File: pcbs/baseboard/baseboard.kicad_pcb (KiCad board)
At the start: 2 copper layers, 86 x 110 mm, 19 parts, among them J1 Power, J3 gpio_breakout, J4 SWD, J5 DC, SW1 SW_Push, U1 Pico

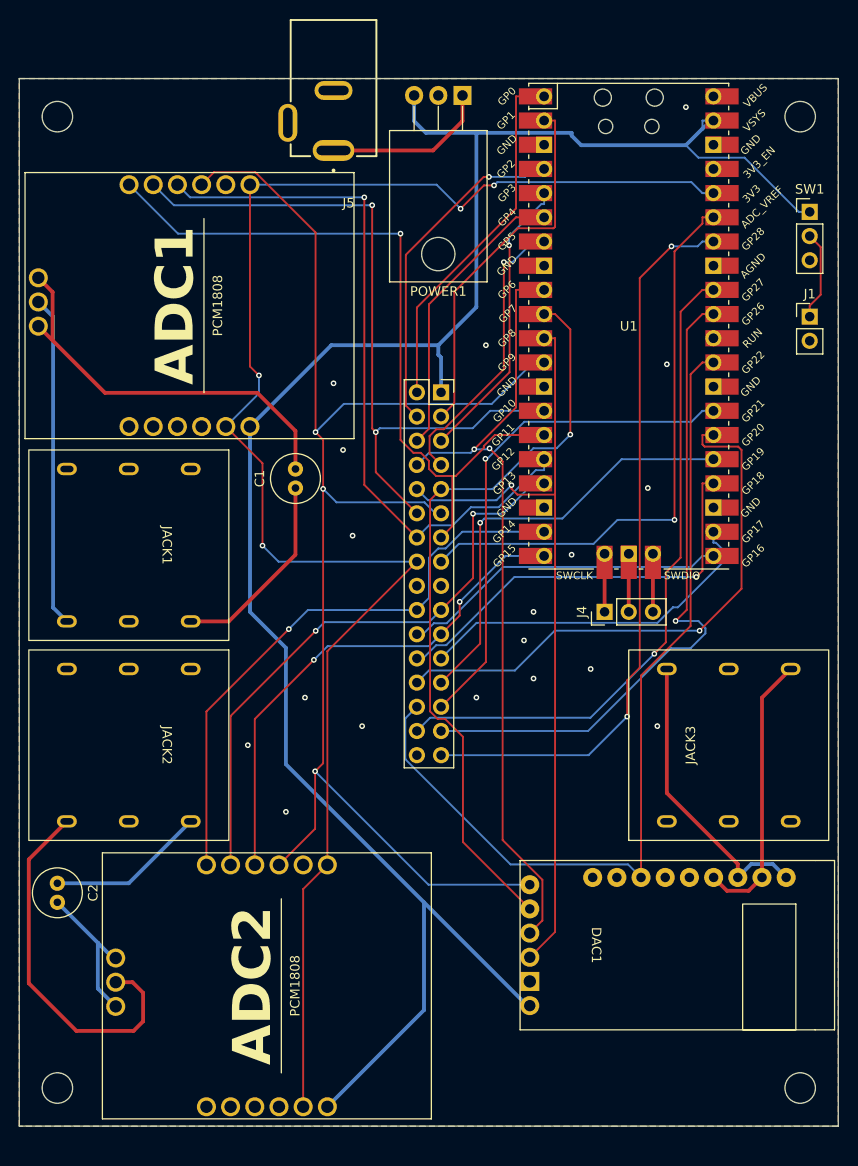
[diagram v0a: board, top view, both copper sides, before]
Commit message: Add devkit and fingybass crates
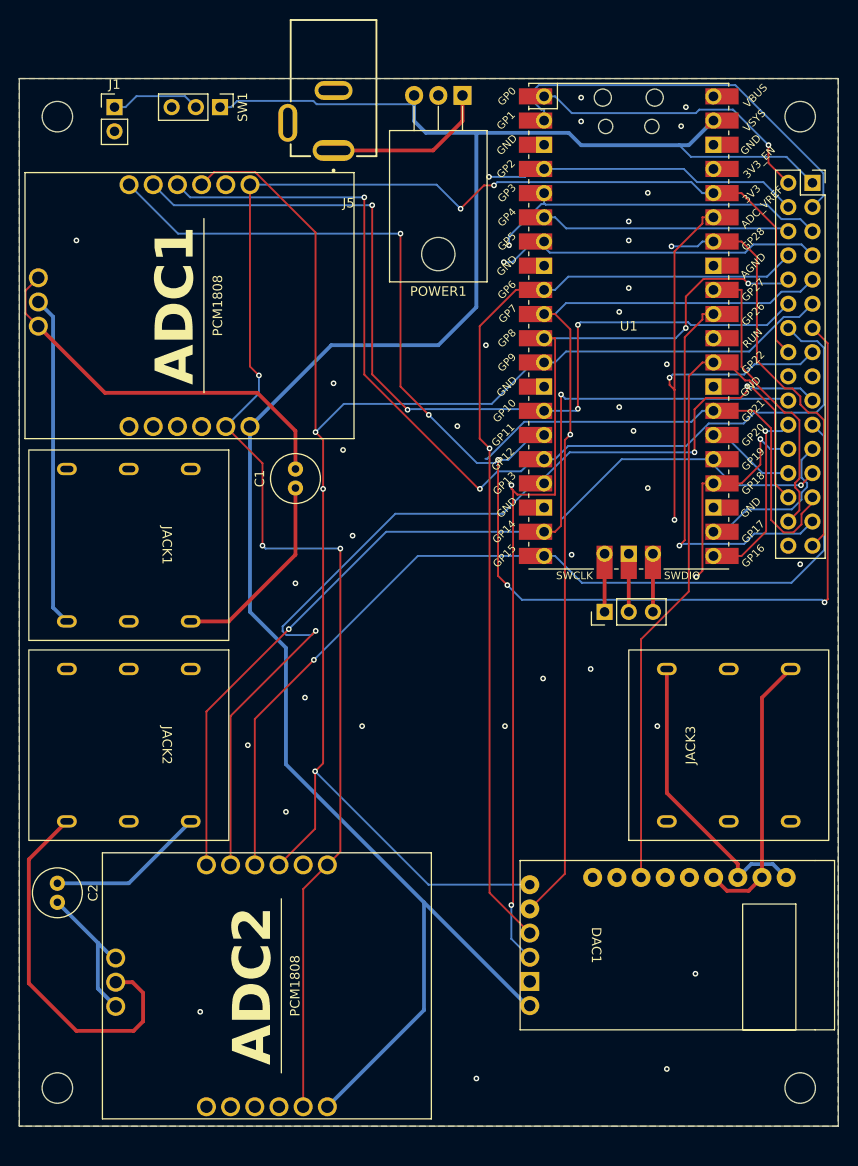
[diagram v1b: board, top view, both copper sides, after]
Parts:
- moved J1 76.2 mm to (150.0, 23.0)
- moved SW1 62.9 mm to (161.1, 23.0), turned to -90 degrees
- moved J3 44.8 mm to (223.3, 30.9)
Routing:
- net /GPIO11: track 78.3 -> 143.5 mm, vias 1 -> 5
- net /GPIO20: track 59.2 -> 9.52 mm, vias 1 -> 0
- net /GPIO15: track 53.6 -> 98.5 mm, vias 2 -> 1
- net /GPIO13: track 62.6 -> 102.8 mm, vias 2 -> 3
- net /GPIO27: track 69.8 -> 31.1 mm, vias 1 -> 0
- net /GPIO14: track 61.9 -> 99.3 mm, vias 1 -> 2
- net /GPIO28: track 77.1 -> 44.5 mm, vias 2 -> 1
- net /GPIO12: track 75.6 -> 106.3 mm, vias 1 -> 2
- net /GPIO26: track 70.5 -> 41.5 mm
- net /GPIO18: track 44.1 -> 23.0 mm, vias 1 -> 2
- net /GPIO17: track 37.7 -> 16.9 mm
- net /GPIO10: track 76.8 -> 97.0 mm, vias 2 -> 4
- net /GPIO8: track 83.5 -> 103.2 mm, vias 1 -> 4
- net /GPIO6: track 83.6 -> 101.5 mm, vias 2 -> 1
- net /GPIO22: track 93.8 -> 76.4 mm
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
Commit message: Expand baseboard + devkit
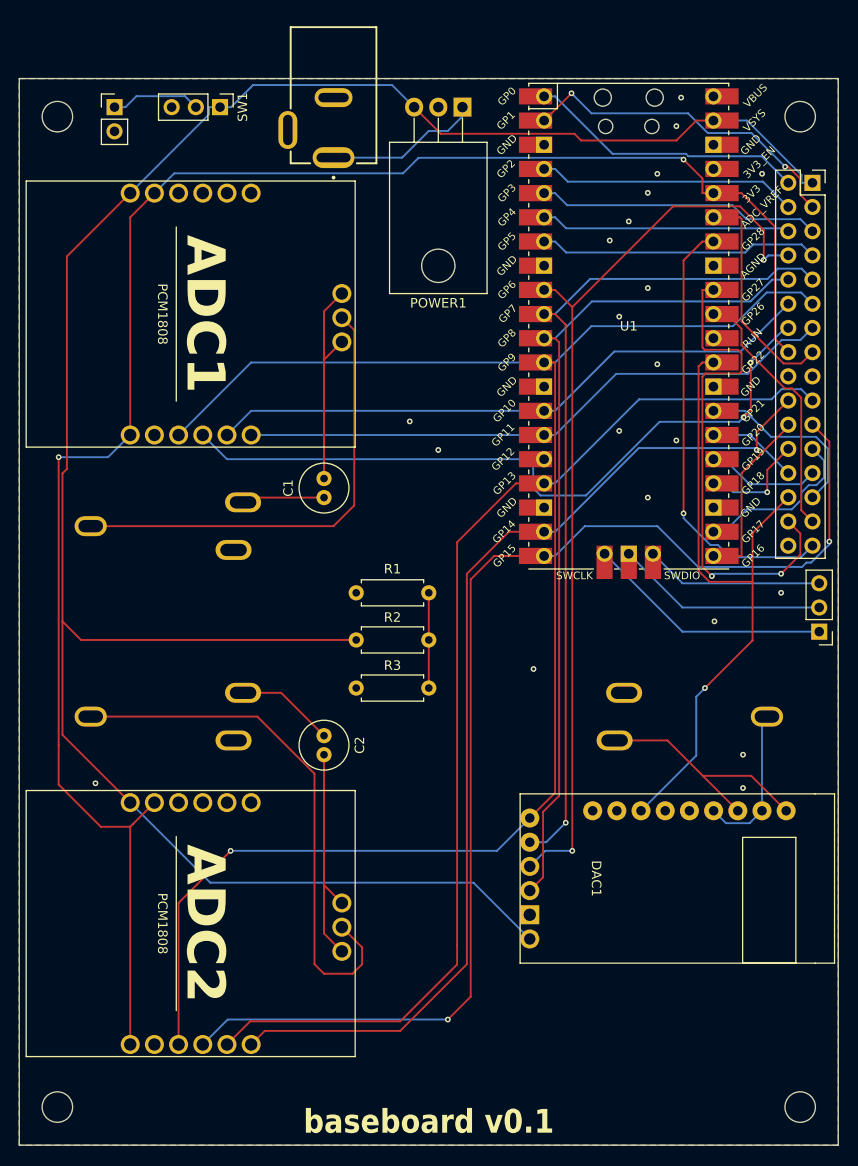
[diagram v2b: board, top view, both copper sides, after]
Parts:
- added R1: 20k, Resistor_THT:R_Axial_DIN0207_L6.3mm_D2.5mm_P7.62mm_Horizontal, F.Cu at (183.0, 74.0)
- added R2: 20k, Resistor_THT:R_Axial_DIN0207_L6.3mm_D2.5mm_P7.62mm_Horizontal, F.Cu at (175.4, 79.0)
- added R3: 100k, Resistor_THT:R_Axial_DIN0207_L6.3mm_D2.5mm_P7.62mm_Horizontal, F.Cu at (175.4, 84.0)
- JACK1, JACK2, JACK3: footprint rytmos:Jack_6.3mm -> rytmos:SlimJack6.3; moved to B.Cu
- moved C2 32.0 mm to (172.0, 89.0)
- moved J4 22.6 mm to (224.0, 78.1), turned to 180 degrees
- moved JACK2 13.3 mm to (157.5, 87.0), turned to 0 degrees
- moved JACK3 13.3 mm to (208.5, 87.0), turned to 180 degrees
- moved JACK1 13.2 mm to (157.5, 67.0), turned to 0 degrees
- moved ADC2 8.94 mm to (158.0, 110.0), turned to -90 degrees
- moved DAC1 7.00 mm to (192.6, 104.0)
- moved ADC1 3.43 mm to (158.0, 46.0), turned to -90 degrees
- moved C1 3.16 mm to (172.0, 64.0)
- moved H3 2.00 mm to (144.0, 128.0)
- moved H4 2.00 mm to (222.0, 128.0)
- moved POWER1 1.23 mm to (186.5, 23.0)
- moved J5 0.75 mm to (173.0, 21.8)
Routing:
- net /GPIO11: track 143.5 -> 63.6 mm, vias 5 -> 0
- net /GPIO10: track 97.0 -> 64.6 mm, vias 4 -> 0
- net /GPIO15: track 98.5 -> 130.1 mm, vias 1 -> 2
- net /GPIO21: track 49.9 -> 19.4 mm
- net /GPIO12: track 106.3 -> 77.3 mm
- net /ADC_VREF: track 51.7 -> 23.6 mm, vias 2 -> 0
- net /GPIO27: track 31.1 -> 53.4 mm, vias 0 -> 2
- net Net-(J4-Pin_1): track 6.10 -> 25.9 mm
- net /GPIO19: track 31.1 -> 12.0 mm, vias 1 -> 0
- net Net-(ADC1-LIN): track 41.7 -> 22.9 mm
- net Net-(ADC2-GIN): track 39.5 -> 56.6 mm
- net Net-(J4-Pin_2): track 6.10 -> 22.3 mm
- net /GPIO8: track 103.2 -> 88.8 mm, vias 4 -> 0
- net /GPIO26: track 41.5 -> 27.3 mm, vias 1 -> 0
- net Net-(ADC1-GIN): track 34.8 -> 48.8 mm
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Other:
- board size 86 x 110 mm -> 86 x 112 mm
- board text added: "baseboard v0.1"

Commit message: Order baseboard and devkit
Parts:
- added JP1: ~, Jumper:SolderJumper-2_P1.3mm_Open_RoundedPad1.0x1.5mm, F.Cu at (162.8, 30.6)
- added JP2: ~, Jumper:SolderJumper-2_P1.3mm_Bridged_RoundedPad1.0x1.5mm, F.Cu at (162.8, 26.6)
- added JP3: ~, Jumper:SolderJumper-2_P1.3mm_Open_RoundedPad1.0x1.5mm, F.Cu at (156.8, 30.6)
- added JP4: ~, Jumper:SolderJumper-2_P1.3mm_Open_RoundedPad1.0x1.5mm, F.Cu at (156.8, 26.6)
- added JP5: ~, Jumper:SolderJumper-2_P1.3mm_Open_RoundedPad1.0x1.5mm, F.Cu at (159.8, 26.6)
- added JP6: ~, Jumper:SolderJumper-2_P1.3mm_Bridged_RoundedPad1.0x1.5mm, F.Cu at (159.8, 30.6)
- J5: moved to B.Cu
- moved J5 0.80 mm to (172.2, 21.8), turned to 0 degrees
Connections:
- J5 pad 1: +9V -> Net-(JP1-A)
- J5 pad 2: unconnected-(J5-Pad2) -> Net-(JP5-A)
- J5 pad 3: GND -> Net-(JP3-A)
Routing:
- net /GPIO11: track 63.6 -> 95.8 mm
- net /GPIO10: track 64.6 -> 95.8 mm
- net /GPIO12: track 77.3 -> 106.1 mm, vias 2 -> 3
- net /GPIO9: track 178.8 -> 205.6 mm, vias 1 -> 0
- net Net-(JP3-A): track 0.00 -> 24.8 mm, vias 0 -> 1
- net +9V: track 16.3 -> 39.2 mm
- net Net-(JP5-A): track 0.00 -> 18.5 mm
- net Net-(JP1-A): track 0.00 -> 12.2 mm
- net +5V: track 232.7 -> 239.1 mm
- net Net-(ADC1-LIN): track 22.9 -> 19.9 mm
- net Net-(ADC2-LIN): track 24.8 -> 22.9 mm
- net /GPIO0: track 29.4 -> 30.8 mm
- net Net-(J1-Pin_1): track 9.49 -> 10.2 mm
- net /GPIO1: track 35.3 -> 34.8 mm
- net GND: vias 20 -> 27
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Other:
- outline, holes or cut-outs redrawn
